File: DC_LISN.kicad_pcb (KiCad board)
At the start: 4 copper layers, 100 x 67.5 mm, 350 parts, among them M1 MountingHole, M2 MountingHole, M3 MountingHole, M4 MountingHole, X1 PCB.SMAFRA.HT, X2 B8B-EH-A, X3 B8B-EH-A, X4 575-4, X5 575-4, X6 575-4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

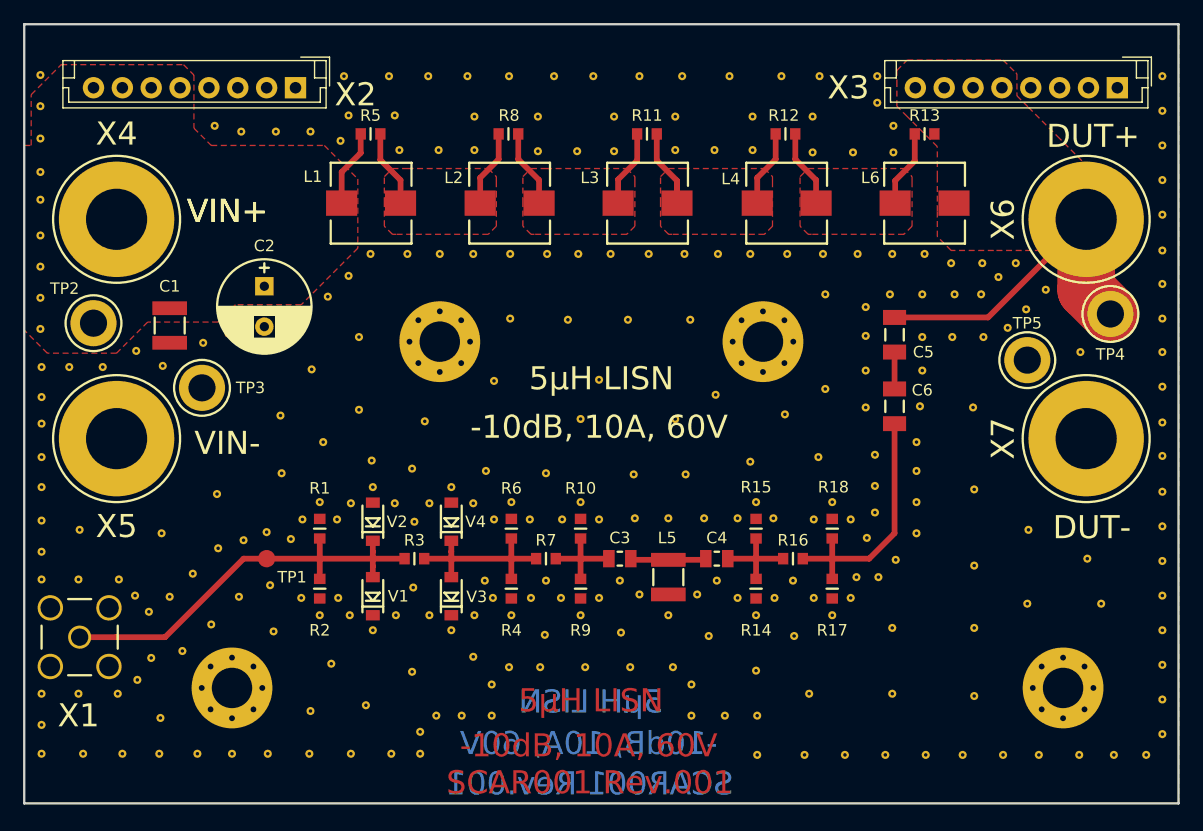
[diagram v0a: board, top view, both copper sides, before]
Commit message: Licensing: Changed to OSHW Changed licensing to open source hardware. Added an additional signal input for use as standalone attenuator.
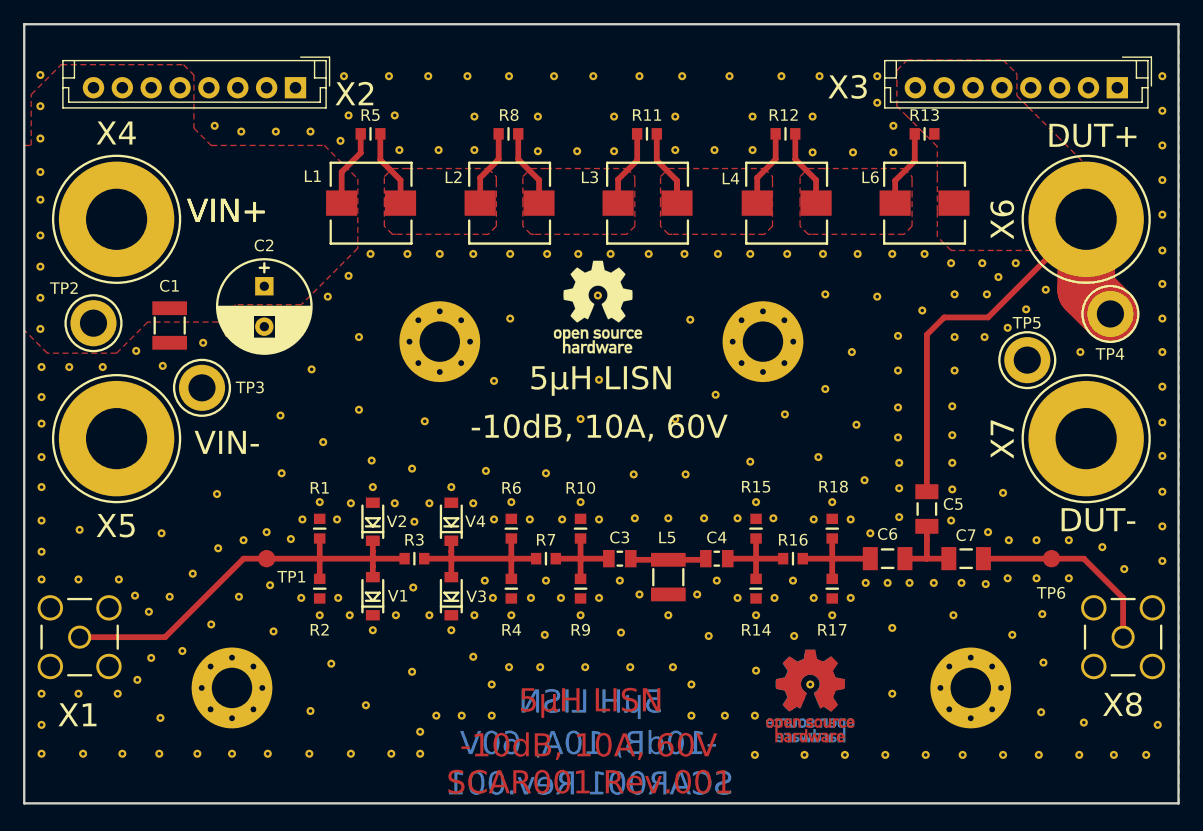
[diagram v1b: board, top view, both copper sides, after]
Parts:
- removed the REF** at (182.3, 109.4)
- removed the REF** at (182.3, 114.8)
- removed the REF** at (182.3, 120.7)
- removed the REF** at (198.6, 115.0)
- removed the REF** at (198.6, 112.0)
- removed the REF** at (198.6, 109.0)
- removed the REF** at (198.6, 106.0)
- removed the REF** at (183.1, 89.6)
- removed the REF** at (182.9, 85.9)
- removed the REF** at (172.9, 87.0)
- removed the REF** at (177.3, 98.7)
- removed the REF** at (177.3, 106.6)
- removed the REF** at (177.3, 103.9)
- removed the REF** at (177.3, 101.2)
- removed the REF** at (173.7, 99.8)
- removed the REF** at (173.7, 102.5)
- removed the REF** at (173.7, 104.8)
- removed the REF** at (192.1, 108.8)
- removed the REF** at (152.3, 88.1)
- removed the REF** at (193.3, 112.7)
- removed the REF** at (186.9, 112.7)
- removed the REF** at (187.0, 106.3)
- removed the REF** at (182.2, 95.7)
- removed the REF** at (182.3, 102.8)
- added C7: 100nF, MST_Lib:C_1206, F.Cu at (181.6, 108.8)
- added REF**: Via_0.3_0.7, MST_Lib:Via_0.3_0.7, F.Cu at (180.5, 113.7)
- added REF**: Via_0.3_0.7, MST_Lib:Via_0.3_0.7, F.Cu at (180.3, 105.5)
- added REF**: Via_0.3_0.7, MST_Lib:Via_0.3_0.7, F.Cu at (191.8, 123.0)
- added REF**: Via_0.3_0.7, MST_Lib:Via_0.3_0.7, F.Cu at (188.1, 122.1)
- added REF**: Via_0.3_0.7, MST_Lib:Via_0.3_0.7, F.Cu at (185.2, 110.5)
- added REF**: Via_0.3_0.7, MST_Lib:Via_0.3_0.7, F.Cu at (190.5, 110.5)
- added REF**: Via_0.3_0.7, MST_Lib:Via_0.3_0.7, F.Cu at (195.3, 109.7)
- added REF**: Via_0.3_0.7, MST_Lib:Via_0.3_0.7, F.Cu at (190.5, 107.2)
- added REF**: Via_0.3_0.7, MST_Lib:Via_0.3_0.7, F.Cu at (187.7, 107.2)
- added REF**: Via_0.3_0.7, MST_Lib:Via_0.3_0.7, F.Cu at (175.7, 98.3)
- added REF**: Via_0.3_0.7, MST_Lib:Via_0.3_0.7, F.Cu at (180.4, 98.1)
- added REF**: Via_0.3_0.7, MST_Lib:Via_0.3_0.7, F.Cu at (173.9, 86.1)
- added REF**: Via_0.3_0.7, MST_Lib:Via_0.3_0.7, F.Cu at (175.8, 100.5)
- added REF**: Via_0.3_0.7, MST_Lib:Via_0.3_0.7, F.Cu at (180.4, 100.5)
- added REF**: Via_0.3_0.7, MST_Lib:Via_0.3_0.7, F.Cu at (193.4, 107.8)
- added REF**: Via_0.3_0.7, MST_Lib:Via_0.3_0.7, F.Cu at (185.3, 107.2)
- added REF**: Via_0.3_0.7, MST_Lib:Via_0.3_0.7, F.Cu at (187.7, 110.5)
- added REF**: Via_0.3_0.7, MST_Lib:Via_0.3_0.7, F.Cu at (181.2, 110.9)
- added REF**: Via_0.3_0.7, MST_Lib:Via_0.3_0.7, F.Cu at (178.8, 110.9)
- added REF**: Via_0.3_0.7, MST_Lib:Via_0.3_0.7, F.Cu at (183.3, 111.0)
- added REF**: Via_0.3_0.7, MST_Lib:Via_0.3_0.7, F.Cu at (185.6, 115.4)
- added REF**: Via_0.3_0.7, MST_Lib:Via_0.3_0.7, F.Cu at (188.3, 117.8)
- added REF**: Via_0.3_0.7, MST_Lib:Via_0.3_0.7, F.Cu at (171.7, 90.9)
- added REF**: Via_0.3_0.7, MST_Lib:Via_0.3_0.7, F.Cu at (188.2, 113.6)
- added REF**: Via_0.3_0.7, MST_Lib:Via_0.3_0.7, F.Cu at (183.5, 106.5)
- added REF**: Via_0.3_0.7, MST_Lib:Via_0.3_0.7, F.Cu at (172.1, 97.2)
- added REF**: Via_0.3_0.7, MST_Lib:Via_0.3_0.7, F.Cu at (172.8, 102.0)
- added REF**: Via_0.3_0.7, MST_Lib:Via_0.3_0.7, F.Cu at (184.8, 103.1)
- added REF**: Via_0.3_0.7, MST_Lib:Via_0.3_0.7, F.Cu at (180.4, 102.8)
- added REF**: Via_0.3_0.7, MST_Lib:Via_0.3_0.7, F.Cu at (175.8, 102.7)
- added REF**: Via_0.3_0.7, MST_Lib:Via_0.3_0.7, F.Cu at (175.8, 105.2)
- added REF***: OSHW-Logo_7.5x8mm_SilkScreen, Symbols:OSHW-Logo_7.5x8mm_SilkScreen, F.Cu at (149.7, 87.0)
- added REF***: OSHW-Logo_7.5x8mm_Copper, Symbols:OSHW-Logo_7.5x8mm_Copper, F.Cu at (168.1, 120.7)
- added REF***: OSHW-Logo_7.5x8mm_Copper, Symbols:OSHW-Logo_7.5x8mm_Copper, B.Cu at (168.1, 120.7)
- added TP6: TEST, MST_Lib:TP_1mm, F.Cu at (189.0, 108.8)
- added X8: PCB.SMAFRA.HT, MST_Lib:X_SMA_THT_Jack_Straight_PCB.SMAFRA.HT, F.Cu at (195.2, 115.6)
- moved C5 15.4 mm to (178.2, 104.5)
- moved C6 13.2 mm to (174.8, 108.8), turned to 180 degrees
- moved REF** 12.0 mm to (198.6, 109.0)
- moved REF** 12.0 mm to (198.6, 106.0)
- moved M3 8.00 mm to (182.0, 120.0)
- moved REF** 3.34 mm to (149.7, 86.0)
- moved REF** 3.13 mm to (177.8, 87.3)
- moved REF** 2.80 mm to (183.4, 85.9)
- moved REF** 2.80 mm to (180.4, 95.6)
- moved REF** 2.80 mm to (180.6, 89.6)
- moved REF** 2.80 mm to (183.2, 89.6)
- moved REF** 2.80 mm to (175.7, 89.5)
- moved REF** 2.80 mm to (180.6, 85.9)
- moved REF** 2.80 mm to (175.7, 92.5)
- moved REF** 2.80 mm to (180.6, 92.5)
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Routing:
- net /SigIn: track 0.00 -> 16.9 mm
- net Net-(C6-Pad2): track 21.9 -> 9.25 mm
- net /DUT+: track 29.2 -> 40.6 mm
- net Net-(C5-Pad2): track 3.20 -> 6.60 mm

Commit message: Layout: Documented Stackup and Impedances
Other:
- board text added: "35µm"
- board text added: "500µm"
- board text added: "50Ohm"
- board text added: "Core 710µm"
- board text added: "Cu"
- board text added: "Impedances"
- board text added: "Layer Stackup"
- board text added: "Midlayer 1"
- board text added: "Prepreg 288µm (2116+7628)"
- board text added: "Prepreg/Core"
- board text added: "Reference Layer"
- board text added: "Signal Layer"
- board text added: "Target Impedance"
- board text added: "Top"
- board text added: "Trace Width"
